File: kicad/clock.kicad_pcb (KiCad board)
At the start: 2 copper layers, 270 x 108 mm, 60 parts, among them J1 USB_C_Receptacle_PowerOnly_6P, J2 USB_A, J5 Barrel_Jack, SW1 SW_SPDT, SW2 SW_Push, SW3 SW_Push, U1 4511, U10 4060, U11 4013, U18 4081, U2 4511, U20 FJS18101APG, U21 FJS18101APG, U22 FJS18101APG, U23 FJS18101APG, U24 FJS18101APG, U25 FJS18101APG, U3 4511, U4 4511, U5 4511, U6 4511, U7 4518, U8 4518, U9 4518, Y1 32768

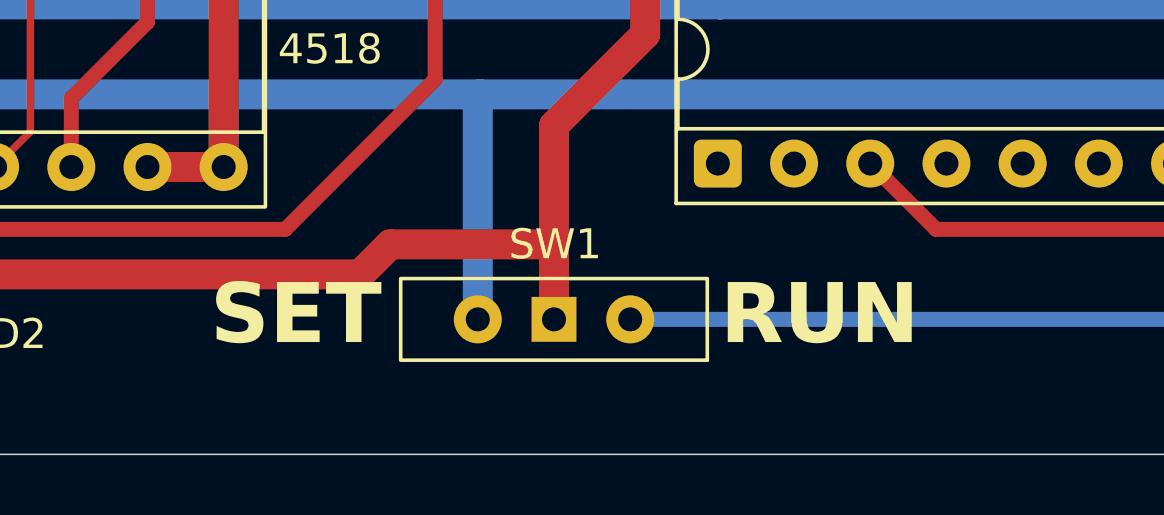
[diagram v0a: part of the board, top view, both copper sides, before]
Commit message: Add QR code
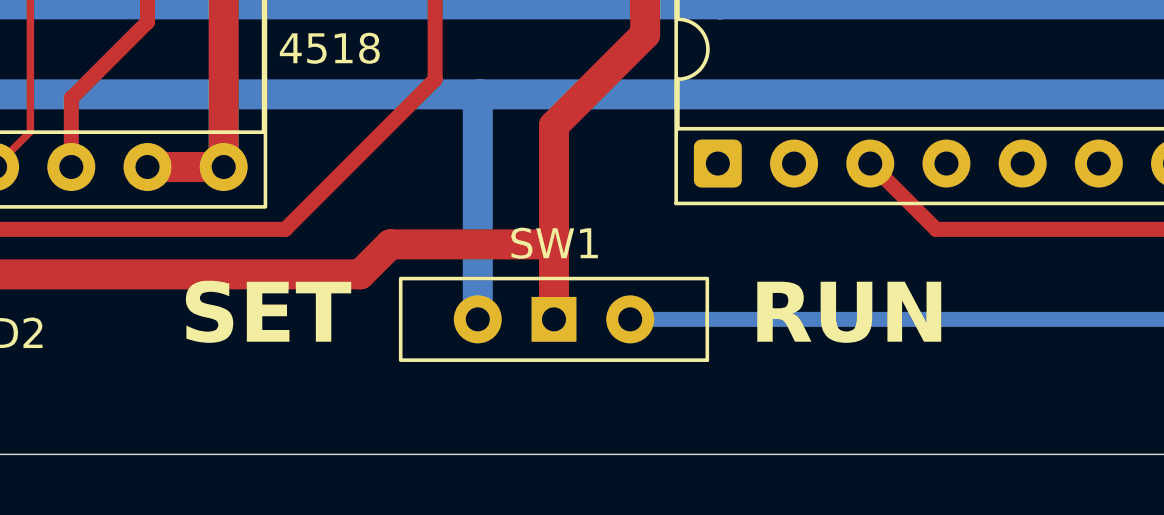
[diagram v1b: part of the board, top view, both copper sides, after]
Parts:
- added G***: LOGO, 80_Bus:qr-code, B.Cu at (289.0, 69.5)
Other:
- board text added: "Docs"

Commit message: Completed article
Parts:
- added H5: MountingHole, MountingHole:MountingHole_3.5mm, F.Cu at (50.0, 95.0)
- added H6: MountingHole, MountingHole:MountingHole_3.5mm, F.Cu at (310.0, 95.0)
- moved G001 48.0 mm to (59.0, 132.0)
- moved J5 26.6 mm to (85.9, 128.3), turned to 0 degrees
- moved U7 14.3 mm to (102.1, 135.6)
- moved D3 13.0 mm to (160.5, 135.5), turned to 90 degrees
- moved D4 11.4 mm to (130.5, 135.7), turned to 90 degrees
- moved D2 8.23 mm to (225.0, 136.0), turned to 90 degrees
- moved D1 8.02 mm to (216.5, 136.0), turned to 90 degrees
- moved SW1 7.87 mm to (256.0, 135.7)
- moved SW2 5.90 mm to (149.0, 131.2)
- moved C3 5.90 mm to (141.8, 127.7)
- moved SW3 5.90 mm to (135.8, 131.2)
- moved C6 5.90 mm to (154.8, 127.7)
- moved J1 5.81 mm to (73.0, 138.4)
- moved H3 5.81 mm to (310.0, 137.2)
- moved H4 5.81 mm to (50.0, 137.2)
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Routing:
- net Net-(U2-DA): track 36.0 -> 59.2 mm
- net Net-(U2-DB): track 19.0 -> 40.0 mm, vias 0 -> 3
- net Net-(U2-DC): track 109.4 -> 128.1 mm, vias 3 -> 2
- net Net-(D3-A): track 48.6 -> 66.7 mm, vias 2 -> 1
- net VDD: track 679.3 -> 662.8 mm, vias 1 -> 4
- net Net-(U2-DD): track 21.9 -> 36.6 mm
- net Net-(D3-K): track 55.3 -> 68.9 mm
- net Net-(U1-DC): track 23.3 -> 11.4 mm, vias 1 -> 0
- net Net-(U7A-Reset): track 98.7 -> 109.9 mm, vias 3 -> 4
- net Net-(U5-DC): track 27.3 -> 37.5 mm
- net Net-(D1-A): track 36.7 -> 28.0 mm, vias 1 -> 0
- net Net-(D2-A): track 96.4 -> 104.0 mm
- net Net-(U1-DA): track 13.6 -> 6.49 mm
- net CLOCK: track 233.5 -> 227.7 mm
- net Net-(RN6-R2.2): track 90.7 -> 86.3 mm
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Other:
- board size 270 x 108 mm -> 269 x 102 mm
- board text added: "V2.1 - Add thicker tracks V3.0 - Revised layout - Improved routing"
- board text added: "V3.0"
- board text added: "b2584150-bdef-42d5-b22f-8ab7f9ebe9e7"
- board text removed: "V2.0"
- board text removed: "bc684f6b-9e58-4770-9e80-08222c1d3e5f"
